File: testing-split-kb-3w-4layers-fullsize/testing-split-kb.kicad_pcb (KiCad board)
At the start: 4 copper layers, 121.5 x 73.1 mm, 37 parts, among them J1 Conn_01x09_Pin, SW1 SW_Push_Dual, SW10 SW_Push_Dual, SW11 SW_Push_Dual, SW12 SW_Push_Dual, SW13 SW_Push_Dual, SW14 SW_Push_Dual, SW15 SW_Push_Dual, SW2 SW_Push_Dual, SW3 SW_Push_Dual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

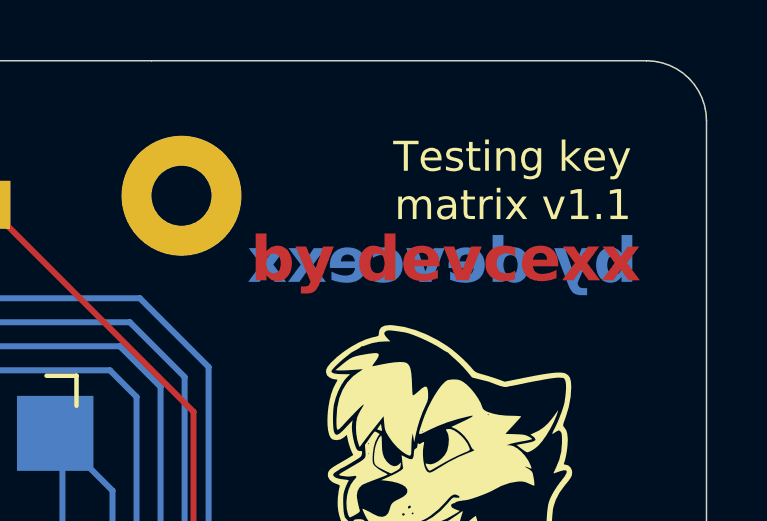
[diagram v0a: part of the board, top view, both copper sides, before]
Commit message: Added multiple new versions of the testing pcb for testing crosstalk with different layouts
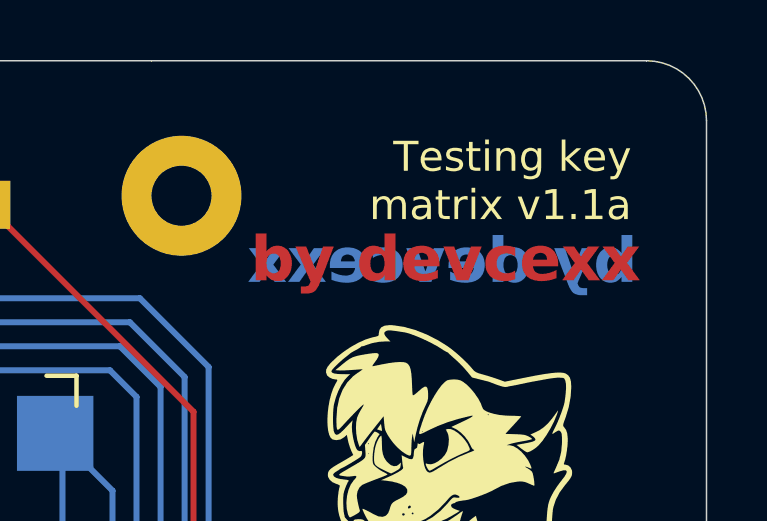
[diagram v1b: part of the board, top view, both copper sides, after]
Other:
- board text added: "Testing key matrix v1.1a"
- board text removed: "Testing key matrix v1.1"
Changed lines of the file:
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@@
 		)
 	)
-	(gr_text "Testing key\nmatrix v1.1"
+	(gr_text "Testing key\nmatrix v1.1a"
 		(at 191.5 37.9 0)
 		(layer "F.SilkS")
@@
 		)
 	)
-	(gr_text "Testing key\nmatrix v1.1"
+	(gr_text "Testing key\nmatrix v1.1a"
 		(at 191.5 37.9 0)
 		(layer "B.SilkS")
